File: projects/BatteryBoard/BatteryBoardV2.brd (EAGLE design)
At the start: 90.5 x 96 mm, 227 parts, among them M1 BSO201SP, SW1 BTS50015-1TAD, SW2 BTS50015-1TAD, T1 AD590FLATPACK, T2 AD590FLATPACK, T3 AD590FLATPACK, T4 AD590FLATPACK, U1 TCA9535PWR, U10 LT1962-3, U11 LT1962-3, U12 LTC4411, U13 LTC4411, U14 LTC4121, U15 VNS3NV04DP-E, U16 LTC4121, U17 VNS3NV04DP-E, U18 AD8418, U19 AD8418, U2 AD7991-0, U3 LTC4412MPS6, U4 LTC4121-4.2, U5 LTC4121-4.2, U6 LC05111C13MTTTG, U7 LC05111C13MTTTG, U8 AD8418, U9 AD8418

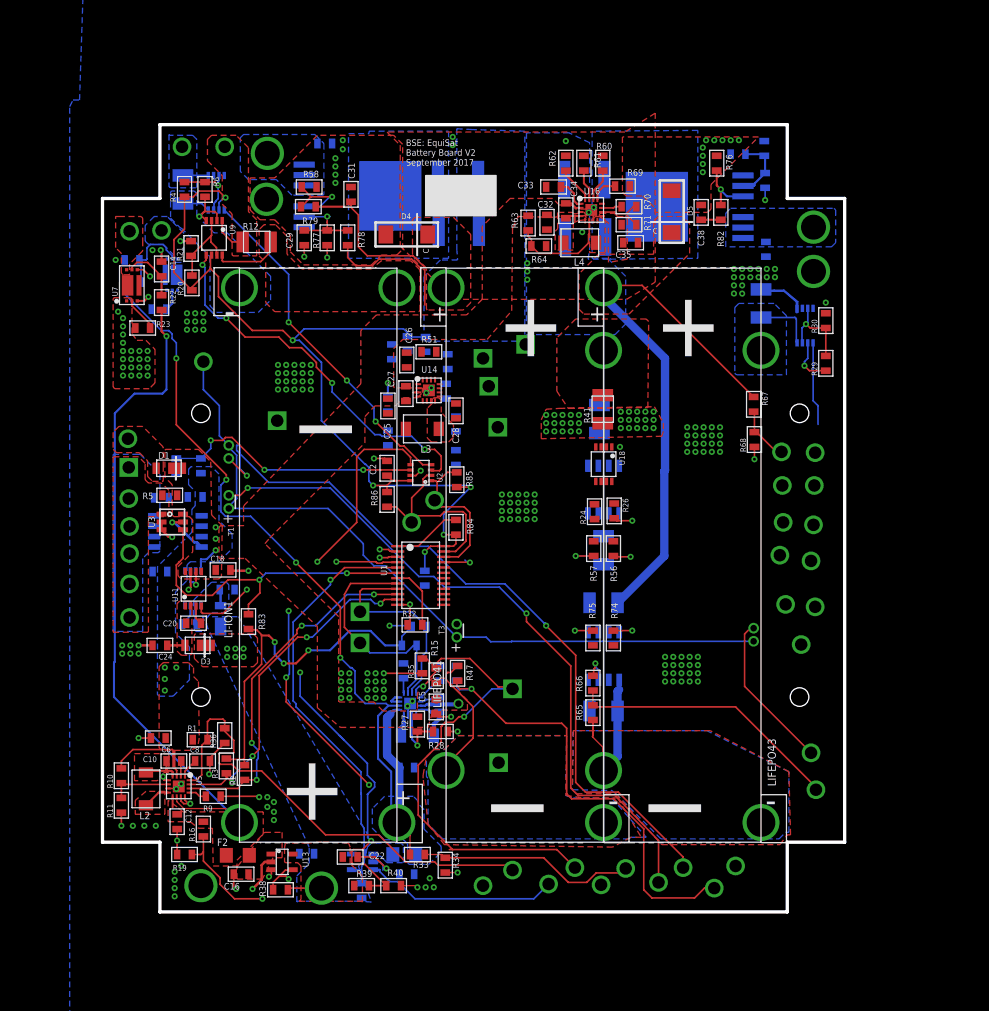
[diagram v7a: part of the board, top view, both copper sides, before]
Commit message: Finished Battery Board V2. Verified all nets connected, silkscreens are readable, axes identified, no overlapping polygons. Created Gerber files, Gerber zip, and schematic pdf.
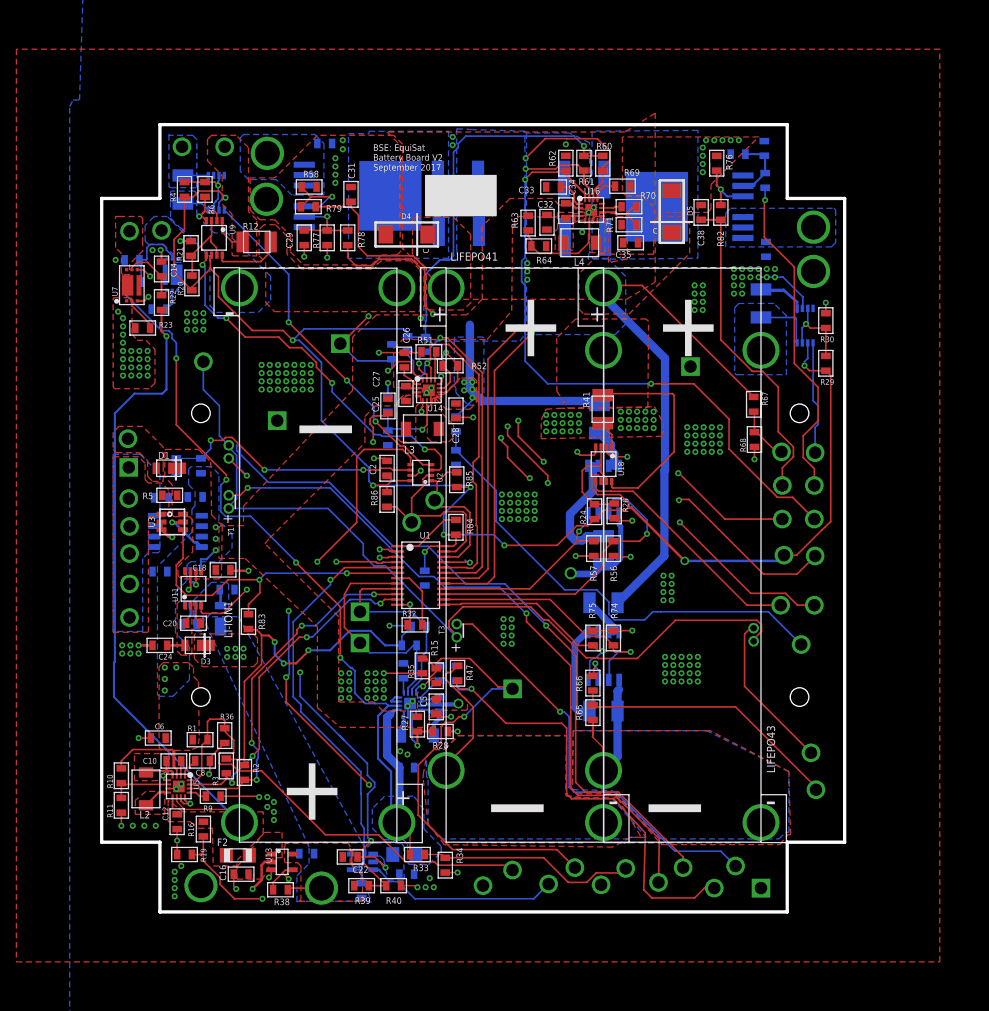
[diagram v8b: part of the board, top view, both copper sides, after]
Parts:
- removed V37: LF_B1_FAULTN, BrownSpaceEngineering:VIA-60MIL-SQ
- removed V38: LIFE1, BrownSpaceEngineering:VIA-60MIL-SQ
- removed V39: LIFE2, BrownSpaceEngineering:VIA-60MIL-SQ
- added V28: GND, BrownSpaceEngineering:VIA-60MIL-SQ
- V22: value LION1_GND+ -> L1_GND+
- V23: value LION1_GND- -> L1_GND-
- V24: value LION2_GND+ -> L2_GND+
- V25: value LION2_GND- -> L2_GND-
- V32, V35: value LF_B1_CHG -> LFB1_CHG
- V36: value LF_B1_CHGN -> GND
- V43: value LF_B1_OUTEN -> LFB1_OUTEN
- V46: value LF_B1_OSNS -> LFB1_OSNS
- V47: value LF_B2_CHG -> LFB2_CHG
- V51: value LF_B2_OUTEN -> LFB2_OUTEN
- V99: value LF_B2_OSNS -> LFB2_OSNS
- moved V36 24.7 mm to (64.7, 66.5), turned to 180 degrees
- moved V32 17.5 mm to (22.0, 69.3)
- moved V43 6.20 mm to (79.9, 43.4)
- moved V35 5.41 mm to (79.8, 37.4)
- moved R52 3.14 mm to (35.4, 66.6), flipped to the top, turned to 0 degrees
- moved V47 0.71 mm to (79.8, 47.9)
- moved V40 0.61 mm to (75.7, 37.4)
- moved R53 0.58 mm to (35.4, 66.6), turned to 180 degrees
- moved V12 0.50 mm to (76.1, 43.5)
- moved V46 0.41 mm to (75.9, 47.9)
- moved C26 0.30 mm to (29.8, 67.3)
- renumbered $6_188_$_2017-09-09_23-53-10 to V99
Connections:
- net GND: now also V28.P$1, V36.P$1
- net LF_B1_BT: now also U1.P$16; no longer U1.P$13
- net LF_B1_CHGN: now also U1.P$20; no longer U1.P$19, V36.P$1
- net LF_B1_FAULTN: now also U1.P$19; no longer U1.P$20, V37.P$1
- net LF_B1_TT: now also U1.P$15; no longer U1.P$14
- net LF_B2_BT: now also U1.P$13; no longer U1.P$16
- net LF_B2_TT: now also U1.P$14; no longer U1.P$15
- net LIFE1: no longer V38.P$1
- net LIFE2: no longer V39.P$1
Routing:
- net +3V3: track 183.5 -> 311.7 mm, vias 11 -> 14
- net LF_B1_CHG: track 0.00 -> 94.0 mm, vias 0 -> 5
- net LF_B2_CHGN: track 3.98 -> 78.9 mm, vias 0 -> 2
- net LF_B2_CHG: track 4.47 -> 77.8 mm, vias 0 -> 2
- net LF_B1_OUTEN: track 17.7 -> 83.9 mm, vias 0 -> 4
- net LF_B2_FAULTN: track 3.77 -> 68.0 mm, vias 0 -> 2
- net LF_B1_OSNS: track 23.9 -> 82.1 mm, vias 0 -> 4
- net LF1_REF: track 0.00 -> 58.1 mm
- net LF1_TEMP: track 0.00 -> 51.3 mm, vias 0 -> 1
- net LF_B1_CHGN: track 0.00 -> 45.9 mm, vias 0 -> 1
- net GND: track 118.9 -> 162.7 mm, vias 271 -> 310
- net LF_B1_FAULTN: track 0.00 -> 42.3 mm, vias 0 -> 2
- net LF_B2_OUTEN: track 1.50 -> 40.4 mm
- net LF_B1_TT: track 0.00 -> 37.7 mm, vias 0 -> 1
- net LF_B2_OSNS: track 2.40 -> 39.8 mm
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- added copper zone on layer 1, net N$30
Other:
- board size 90.5 x 96 mm -> 90.6 x 96 mm
